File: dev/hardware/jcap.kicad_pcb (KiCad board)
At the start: 2 copper layers, 149.1 x 77 mm, 74 parts, among them J201 CPU PGMR, J202 GPU PGMR, J203 SPARE GPU HDR, J204 SPARE CPU HDR, J301 DC IN, J502 VGA OUT, J601 CONTROLS, SW201 CPU ~{RES}, SW202 GPU ~{RES}, SW203 DEBUG, SW601 TILT, U101 P8X32A-D40, U201 P8X32A-D40, U302 LF33_TO220, U401 24LC256, U402 24LC256, U601 74HC165, U602 74HC165, Y101 6.5MHz, Y201 6.5MHz

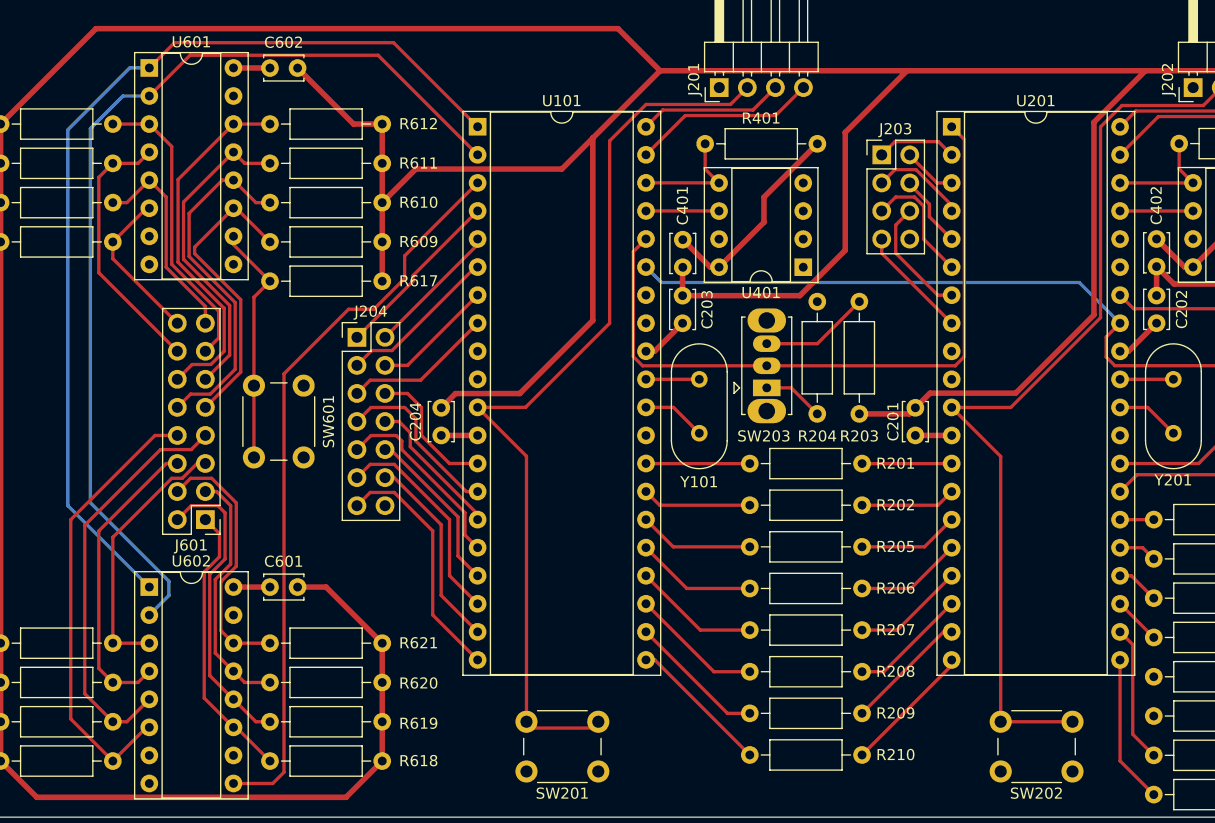
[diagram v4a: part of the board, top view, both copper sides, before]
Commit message: Fixed lib footprint 3D model refs
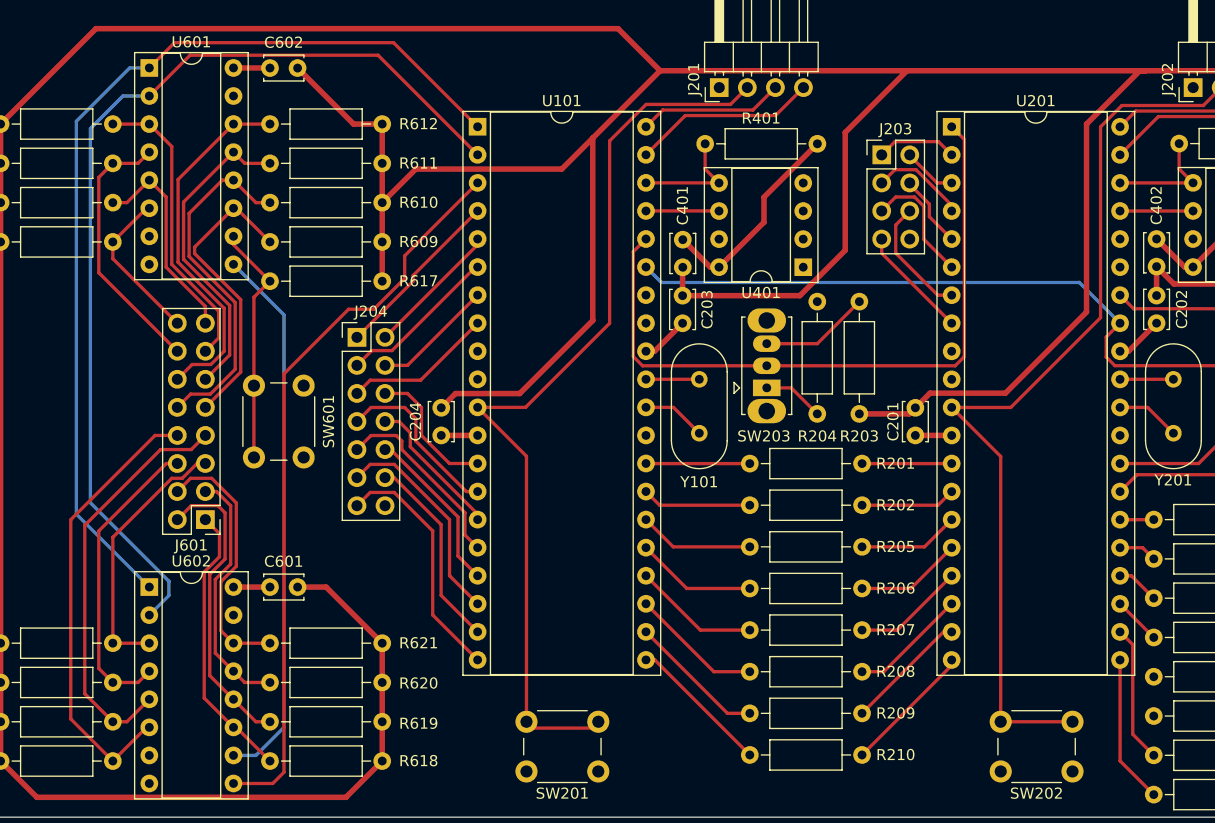
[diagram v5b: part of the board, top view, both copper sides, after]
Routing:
- net /Input/SHIFT_IN: track 0.00 -> 49.4 mm
- net ~{INPUTS_PL}: track 88.0 -> 87.3 mm
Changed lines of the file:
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@@
     (pad "3" thru_hole oval (at 4 0 90) (size 1.5 2.5) (drill 0.8) (layers "*.Cu" "*.Mask")
       (net 46 "Net-(SW203-C)") (pinfunction "C") (pintype "passive"))
-    (model "C:/Users/Connor/Downloads/OS102011MS2QN1--3DModel-STEP-1.STEP"
-      (offset (xyz 2 0 4))
-      (scale (xyz 1 1 1))
-      (rotate (xyz -90 0 0))
+    (model "${KICAD6_3DMODEL_DIR}/Button_Switch_THT.3dshapes/SW_Slide_1P2T_CK_OS102011MS2Q.wrl"
+      (offset (xyz 0 0 0))
+      (scale (xyz 1 1 1))
+      (rotate (xyz 0 0 0))
     )
   )
@@
     (pad "MP" thru_hole circle (at 4.5 7 90) (size 3.5 3.5) (drill 2.5) (layers "*.Cu" "*.Mask")
       (net 4 "GND") (pinfunction "MountPin") (pintype "passive"))
-    (model "C:/Users/Connor/Downloads/CUI_DEVICES_PJ-063AH.step"
-      (offset (xyz 0 -12 5))
-      (scale (xyz 1 1 1))
-      (rotate (xyz -90 0 0))
+    (model "${KICAD6_3DMODEL_DIR}/Connector_BarrelJack.3dshapes/BarrelJack_CUI_PJ-063AH_Horizontal_CircularHoles.wrl"
+      (offset (xyz 0 0 0))
+      (scale (xyz 1 1 1))
+      (rotate (xyz 0 0 0))
     )
   )
@@
   (segment (start 95.758 137.414) (end 99.04 140.696) (width 0.5) (layer "F.Cu") (net 1))
   (segment (start 215.646 78.709761) (end 211.866239 74.93) (width 0.5) (layer "F.Cu") (net 1))
-  (segment (start 194.726 79.594) (end 199.39 74.93) (width 0.5) (layer "F.Cu") (net 1))
+  (segment (start 178.562 105.44) (end 179.887 104.115) (width 0.5) (layer "F.Cu") (net 1))
   (segment (start 215.646 81.534) (end 215.646 78.709761) (width 0.5) (layer "F.Cu") (net 1))
-  (segment (start 187.644472 104.115) (end 179.887 104.115) (width 0.5) (layer "F.Cu") (net 1))
   (segment (start 104.394 71.12) (end 151.648 71.12) (width 0.5) (layer "F.Cu") (net 1))
+  (segment (start 186.715 104.115) (end 194.056 96.774) (width 0.5) (layer "F.Cu") (net 1))
   (segment (start 200.396 92.66) (end 201.97 94.234) (width 0.5) (layer "F.Cu") (net 1))
   (segment (start 157.49 95.29) (end 168.108 95.29) (width 0.5) (layer "F.Cu") (net 1))
   (segment (start 229.636 84.602) (end 225.806 84.602) (width 0.5) (layer "F.Cu") (net 1))
   (segment (start 218.714 84.602) (end 215.646 81.534) (width 0.5) (layer "F.Cu") (net 1))
-  (segment (start 187.644472 104.115) (end 194.726 97.033472) (width 0.5) (layer "F.Cu") (net 1))
+  (segment (start 194.056 96.774) (end 194.056 79.756) (width 0.5) (layer "F.Cu") (net 1))
   (segment (start 200.396 95.28) (end 200.396 92.66) (width 0.5) (layer "F.Cu") (net 1))
   (segment (start 149.362 81.026) (end 155.458 74.93) (width 0.5) (layer "F.Cu") (net 1))
@@
   (segment (start 155.458 74.93) (end 199.39 74.93) (width 0.5) (layer "F.Cu") (net 1))
   (segment (start 212.09 94.234) (end 215.646 90.678) (width 0.5) (layer "F.Cu") (net 1))
-  (segment (start 179.887 104.115) (end 178.562 105.44) (width 0.5) (layer "F.Cu") (net 1))
+  (segment (start 179.887 104.115) (end 186.715 104.115) (width 0.5) (layer "F.Cu") (net 1))
   (segment (start 127.02 140.696) (end 130.302 137.414) (width 0.5) (layer "F.Cu") (net 1))
+  (segment (start 194.056 79.756) (end 198.882 74.93) (width 0.5) (layer "F.Cu") (net 1))
   (segment (start 130.302 79.756) (end 127.712 79.756) (width 0.5) (layer "F.Cu") (net 1))
   (segment (start 127.712 79.756) (end 122.642 74.686) (width 0.5) (layer "F.Cu") (net 1))
@@
   (segment (start 136.936 104.15) (end 142.748 104.15) (width 0.5) (layer "F.Cu") (net 1))
   (segment (start 157.49 92.74) (end 157.51 92.72) (width 0.5) (layer "F.Cu") (net 1))
-  (segment (start 194.726 97.033472) (end 194.726 79.594) (width 0.5) (layer "F.Cu") (net 1))
   (segment (start 99.04 140.696) (end 127.02 140.696) (width 0.5) (layer "F.Cu") (net 1))
   (segment (start 130.302 86.868) (end 133.34 83.83) (width 0.5) (layer "F.Cu") (net 1))
   (segment (start 133.34 83.83) (end 146.558 83.83) (width 0.5) (layer "F.Cu") (net 1))
+  (segment (start 198.882 74.93) (end 199.39 74.93) (width 0.5) (layer "F.Cu") (net 1))
   (segment (start 135.646 105.44) (end 136.936 104.15) (width 0.5) (layer "F.Cu") (net 1))
   (segment (start 95.758 79.756) (end 104.394 71.12) (width 0.5) (layer "F.Cu") (net 1))
@@
   (segment (start 111.506 72.39) (end 131.328 72.39) (width 0.3) (layer "F.Cu") (net 77))
   (segment (start 131.328 72.39) (end 138.938 80) (width 0.3) (layer "F.Cu") (net 77))
-  (segment (start 107.442 74.676) (end 101.854 80.264) (width 0.3) (layer "B.Cu") (net 77))
+  (segment (start 107.442 74.676) (end 102.616 79.502) (width 0.3) (layer "B.Cu") (net 77))
+  (segment (start 102.616 79.502) (end 102.616 115.062) (width 0.3) (layer "B.Cu") (net 77))
   (segment (start 109.22 74.676) (end 107.442 74.676) (width 0.3) (layer "B.Cu") (net 77))
-  (segment (start 101.854 114.3) (end 109.22 121.666) (width 0.3) (layer "B.Cu") (net 77))
-  (segment (start 101.854 80.264) (end 101.854 114.3) (width 0.3) (layer "B.Cu") (net 77))
+  (segment (start 102.616 115.062) (end 109.22 121.666) (width 0.3) (layer "B.Cu") (net 77))
   (segment (start 109.22 77.216) (end 112.91 73.526) (width 0.3) (layer "F.Cu") (net 78))
   (segment (start 129.924 73.526) (end 138.938 82.54) (width 0.3) (layer "F.Cu") (net 78))
@@
   (segment (start 203.693 87.625) (end 203.698 87.62) (width 0.3) (layer "F.Cu") (net 91))
   (segment (start 197.089 87.625) (end 203.693 87.625) (width 0.3) (layer "F.Cu") (net 91))
+  (segment (start 121.412 97.028) (end 121.412 134.366) (width 0.3) (layer "B.Cu") (net 93))
+  (segment (start 118.872 136.906) (end 116.84 136.906) (width 0.3) (layer "B.Cu") (net 93))
+  (segment (start 121.412 134.366) (end 118.872 136.906) (width 0.3) (layer "B.Cu") (net 93))
+  (segment (start 116.84 92.456) (end 121.412 97.028) (width 0.3) (layer "B.Cu") (net 93))
   (segment (start 116.84 90.678) (end 116.84 89.916) (width 0.3) (layer "F.Cu") (net 94))
   (segment (start 118.69 103.435) (end 118.69 95.432) (width 0.3) (layer "F.Cu") (net 94))

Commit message: Nearly final PCB
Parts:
- moved D301 100.5 mm to (133.6, 128.8), turned to 180 degrees
- moved J301 98.2 mm to (136.0, 140.1), turned to 0 degrees
- moved U302 96.7 mm to (150.1, 144.3), turned to -90 degrees
- moved C301 93.4 mm to (145.3, 139.5), turned to -90 degrees
- moved C302 92.3 mm to (150.1, 140.0)
- moved R301 89.9 mm to (143.3, 134.9), turned to 180 degrees
- moved SW201 68.0 mm to (155.6, 70.6), turned to 0 degrees
- moved SW202 68.0 mm to (198.5, 70.6), turned to 0 degrees
- moved R512 50.2 mm to (213.4, 147.3), turned to 90 degrees
- moved C601 47.1 mm to (112.8, 75.2)
- moved R619 47.1 mm to (112.8, 87.4)
- moved R620 47.1 mm to (112.8, 83.8)
- moved R621 47.1 mm to (112.8, 80.3)
- moved R622 47.1 mm to (98.6, 80.3)
- moved R623 47.1 mm to (98.6, 83.8)
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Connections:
- J601 pad 10: /Input/IN10 -> /Input/IN13
- J601 pad 11: /Input/IN11 -> /Input/IN6
- J601 pad 12: /Input/IN12 -> /Input/IN14
- J601 pad 13: /Input/IN13 -> /Input/IN7
- J601 pad 14: /Input/IN14 -> /Input/IN15
- J601 pad 15: /Input/IN15 -> /Input/IN8
- J601 pad 2: /Input/IN2 -> /Input/IN9
- J601 pad 3: /Input/IN3 -> /Input/IN2
- J601 pad 4: /Input/IN4 -> /Input/IN10
- J601 pad 5: /Input/IN5 -> /Input/IN3
- J601 pad 6: /Input/IN6 -> /Input/IN11
- J601 pad 7: /Input/IN7 -> /Input/IN4
- J601 pad 8: /Input/IN8 -> /Input/IN12
- J601 pad 9: /Input/IN9 -> /Input/IN5
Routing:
- net +3.3V: track 471.3 -> 838.7 mm
- net ~{INPUTS_PL}: track 87.3 -> 138.4 mm
- net V_SYNC: track 60.2 -> 104.0 mm
- net H_SYNC: track 10.5 -> 53.1 mm
- net INPUTS_CLK: track 89.3 -> 130.0 mm
- net /Propellers/~{SER_RES_CPU}: track 83.4 -> 48.9 mm
- net /Propellers/~{SER_RES_GPU}: track 83.3 -> 49.8 mm
- net /Input/IN8: track 40.8 -> 18.8 mm
- net /Input/IN16: track 14.3 -> 34.1 mm
- net /Input/SHIFT_IN: track 49.4 -> 66.9 mm
- net Net-(J502-Pad14): track 38.3 -> 21.9 mm
- net /VGA_DAC/BLUE_OUT: track 25.9 -> 10.9 mm
- net /Propellers/DEBUG: track 63.1 -> 75.9 mm
- net /Input/IN9: track 27.1 -> 38.4 mm
- net /Input/IN15: track 19.2 -> 30.2 mm
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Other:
- board size 149.1 x 77 mm -> 140 x 87 mm
